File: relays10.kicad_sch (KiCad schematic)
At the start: 1 part

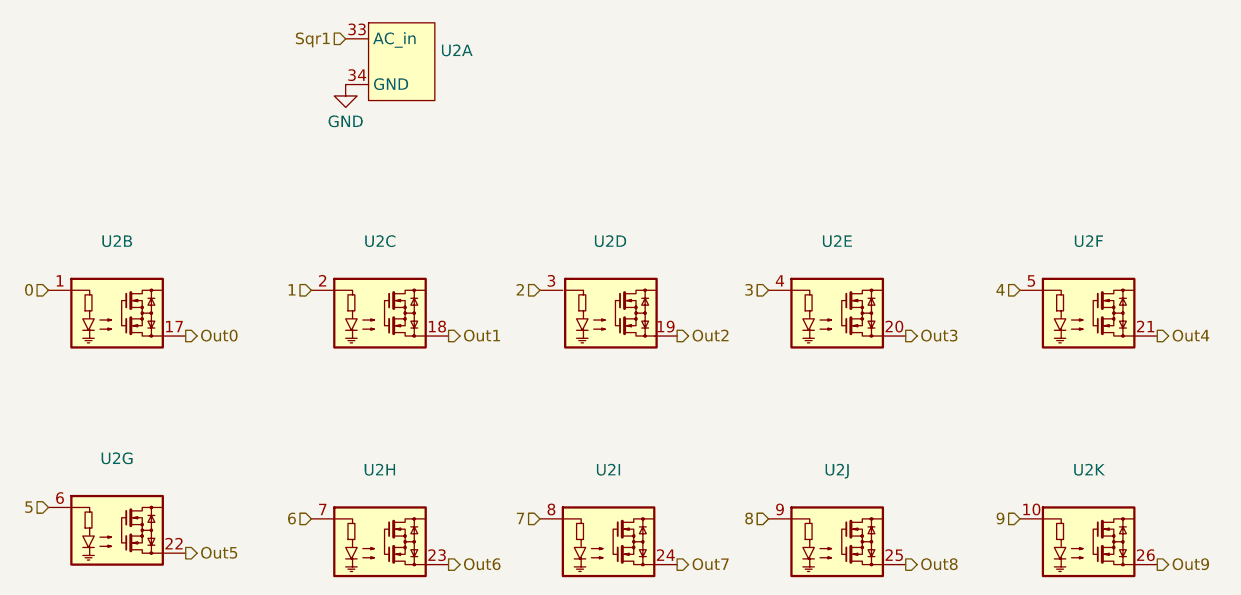
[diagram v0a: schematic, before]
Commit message: added module for PSU
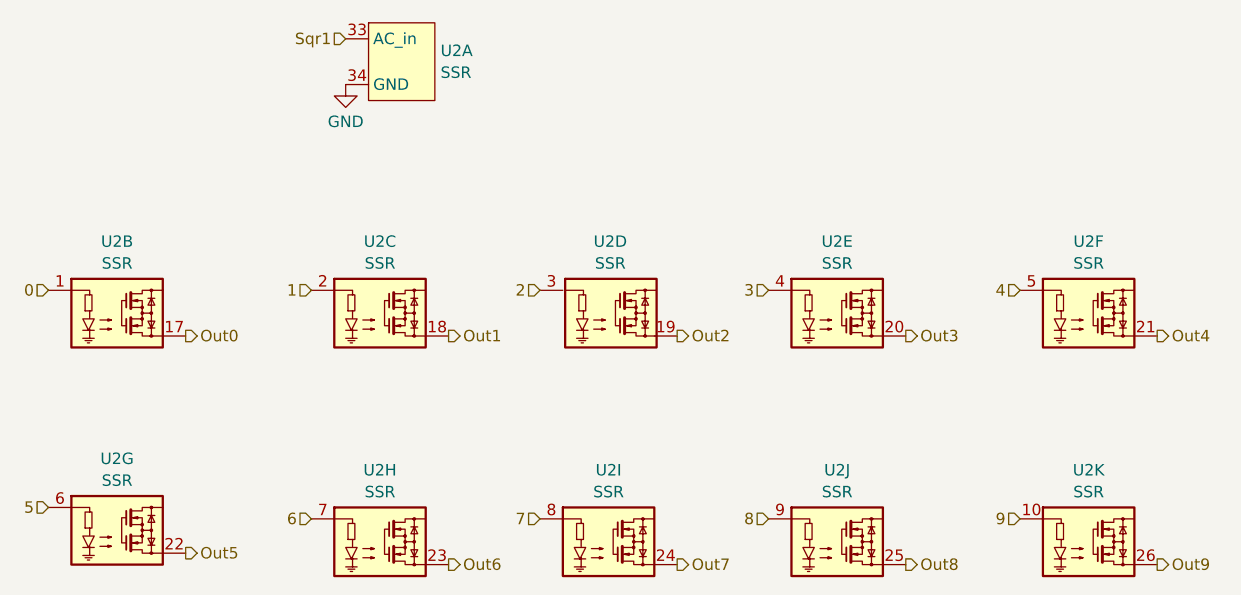
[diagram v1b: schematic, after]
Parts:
- U2: value ~ -> SSR
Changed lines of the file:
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@@
 			)
 		)
-		(property "Value" "~"
+		(property "Value" "SSR"
 			(at 152.4 103.6898 0)
 			(effects
@@
 				)
 				(path "/ce10d5bc-995e-4952-aa76-0a08f713a0f2/2c36a9e9-de42-4705-9ad4-94f4cc168e2f/c88a1bac-4a06-4b38-bc9b-1c7c792dec41"
-					(reference "U9")
+					(reference "U3")
 					(unit 10)
 				)
@@
 			)
 		)
-		(property "Value" "~"
+		(property "Value" "SSR"
 			(at 72.39 78.2898 0)
 			(effects
@@
 				)
 				(path "/ce10d5bc-995e-4952-aa76-0a08f713a0f2/2c36a9e9-de42-4705-9ad4-94f4cc168e2f/c88a1bac-4a06-4b38-bc9b-1c7c792dec41"
-					(reference "U9")
+					(reference "U3")
 					(unit 2)
 				)
@@
 			)
 		)
-		(property "Value" "~"
+		(property "Value" "SSR"
 			(at 101.6 103.6898 0)
 			(effects
@@
 				)
 				(path "/ce10d5bc-995e-4952-aa76-0a08f713a0f2/2c36a9e9-de42-4705-9ad4-94f4cc168e2f/c88a1bac-4a06-4b38-bc9b-1c7c792dec41"
-					(reference "U9")
+					(reference "U3")
 					(unit 8)
 				)
@@
 			)
 		)
-		(property "Value" "~"
+		(property "Value" "SSR"
 			(at 101.6 78.2898 0)
 			(effects
@@
 				)
 				(path "/ce10d5bc-995e-4952-aa76-0a08f713a0f2/2c36a9e9-de42-4705-9ad4-94f4cc168e2f/c88a1bac-4a06-4b38-bc9b-1c7c792dec41"
-					(reference "U9")
+					(reference "U3")
 					(unit 3)
 				)
@@
 			)
 		)
-		(property "Value" "~"
+		(property "Value" "SSR"
 			(at 108.331 57.0921 0)
 			(effects
@@
 				)
 				(path "/ce10d5bc-995e-4952-aa76-0a08f713a0f2/2c36a9e9-de42-4705-9ad4-94f4cc168e2f/c88a1bac-4a06-4b38-bc9b-1c7c792dec41"
-					(reference "U9")
+					(reference "U3")
 					(unit 1)
 				)
@@
 			)
 		)
-		(property "Value" "~"
+		(property "Value" "SSR"
 			(at 180.34 103.6898 0)
 			(effects
@@
 				)
 				(path "/ce10d5bc-995e-4952-aa76-0a08f713a0f2/2c36a9e9-de42-4705-9ad4-94f4cc168e2f/c88a1bac-4a06-4b38-bc9b-1c7c792dec41"
-					(reference "U9")
+					(reference "U3")
 					(unit 11)
 				)
@@
 			)
 		)
-		(property "Value" "~"
+		(property "Value" "SSR"
 			(at 180.34 78.2898 0)
 			(effects
@@
 				)
 				(path "/ce10d5bc-995e-4952-aa76-0a08f713a0f2/2c36a9e9-de42-4705-9ad4-94f4cc168e2f/c88a1bac-4a06-4b38-bc9b-1c7c792dec41"
-					(reference "U9")
+					(reference "U3")
 					(unit 6)
 				)
@@
 			)
 		)
-		(property "Value" "~"
+		(property "Value" "SSR"
 			(at 72.39 102.4198 0)
 			(effects
@@
 				)
 				(path "/ce10d5bc-995e-4952-aa76-0a08f713a0f2/2c36a9e9-de42-4705-9ad4-94f4cc168e2f/c88a1bac-4a06-4b38-bc9b-1c7c792dec41"
-					(reference "U9")
+					(reference "U3")
 					(unit 7)
 				)
@@
 			)
 		)
-		(property "Value" "~"
+		(property "Value" "SSR"
 			(at 127 103.6898 0)
 			(effects
@@
 				)
 				(path "/ce10d5bc-995e-4952-aa76-0a08f713a0f2/2c36a9e9-de42-4705-9ad4-94f4cc168e2f/c88a1bac-4a06-4b38-bc9b-1c7c792dec41"
-					(reference "U9")
+					(reference "U3")
 					(unit 9)
 				)
@@
 			)
 		)
-		(property "Value" "~"
+		(property "Value" "SSR"
 			(at 127.1905 78.2898 0)
 			(effects
@@
 				)
 				(path "/ce10d5bc-995e-4952-aa76-0a08f713a0f2/2c36a9e9-de42-4705-9ad4-94f4cc168e2f/c88a1bac-4a06-4b38-bc9b-1c7c792dec41"
-					(reference "U9")
+					(reference "U3")
 					(unit 4)
 				)
@@
 			)
 		)
-		(property "Value" "~"
+		(property "Value" "SSR"
 			(at 152.4 78.2898 0)
 			(effects
@@
 				)
 				(path "/ce10d5bc-995e-4952-aa76-0a08f713a0f2/2c36a9e9-de42-4705-9ad4-94f4cc168e2f/c88a1bac-4a06-4b38-bc9b-1c7c792dec41"
-					(reference "U9")
+					(reference "U3")
 					(unit 5)
 				)
